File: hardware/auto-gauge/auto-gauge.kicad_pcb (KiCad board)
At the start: 2 copper layers, 48.6 x 48.3 mm, 41 parts

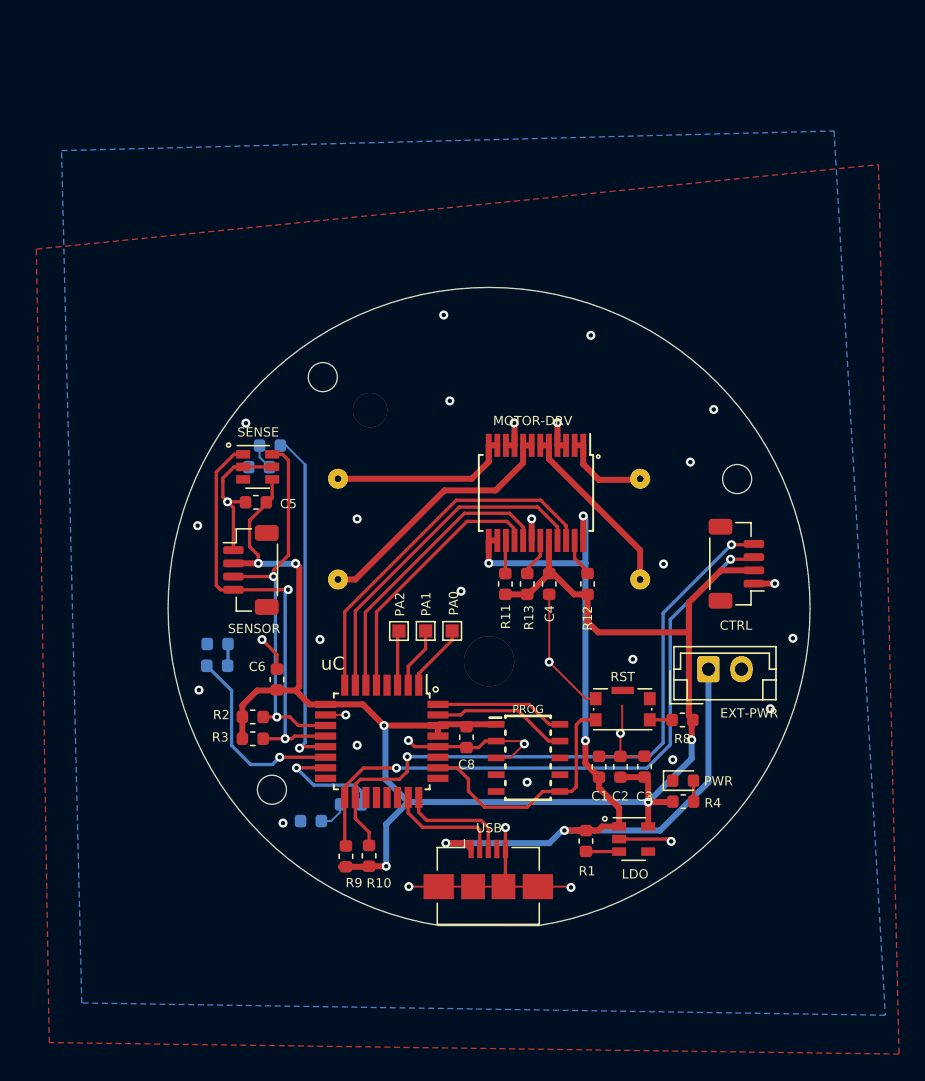
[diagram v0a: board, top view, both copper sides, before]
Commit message: arduino dummy/test. New board using atmega328 for jlcpcb asm
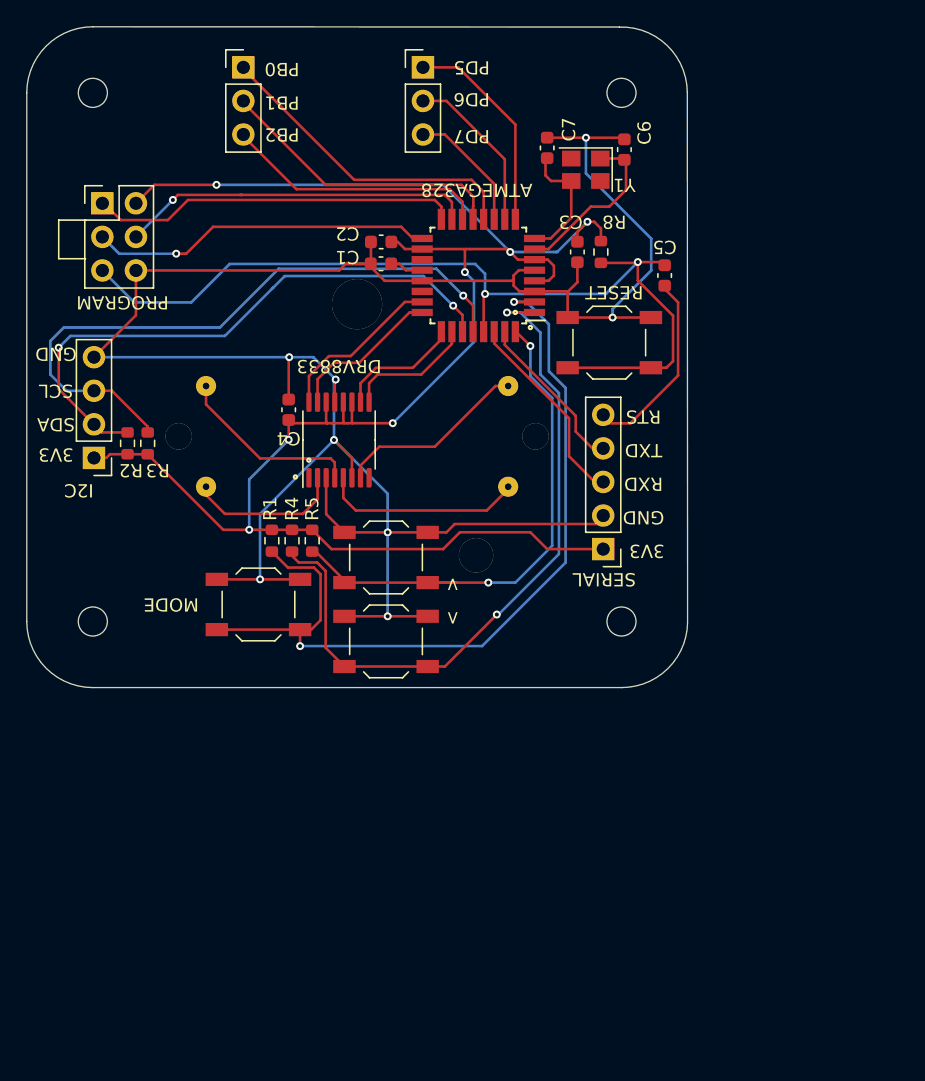
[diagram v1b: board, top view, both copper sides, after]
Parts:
- removed C8: 1uF, Capacitor_SMD:C_0603_1608Metric
- removed CTRL: CONN_04JST-SH, Connector_JST:JST_SH_BM04B-SRSS-TB_1x04-1MP_P1.00mm_Vertical
- removed D1, D2, D3, PWR: LED, LED_SMD:LED_0603_1608Metric
- removed EXT-PWR: JST Vertical Header, Connector_JST:JST_EH_B2B-EH-A_1x02_P2.50mm_Vertical
- removed Gauge: Stepper_Motor_bipolar, auto-gauge:Auto-Stepper-Test
- removed LDO: SPX3819M5-L-3-3, Package_TO_SOT_SMD:SOT-23-5
- removed MOTOR-DRV: TB6612FNG, Package_SO:SSOP-24_5.3x8.2mm_P0.65mm
- removed PA0, PA1, PA2: TestPoint, TestPoint:TestPoint_Pad_1.0x1.0mm
- removed PROG: CORTEX_DEBUG_SMD, sf:SAMTECH_FTSH-105-01
- removed R10, R9: 4.7k, Resistor_SMD:R_0603_1608Metric
- removed R11, R12, R13: 10k, Resistor_SMD:R_0603_1608Metric
- removed R6, R7: 1.5k, Resistor_SMD:R_0603_1608Metric
- removed RST: SW_Push, Button_Switch_SMD:SW_Push_1P1T-SH_NO_CK_KMR2xxG
- removed SENSE: TMP101, Package_TO_SOT_SMD:SOT-23-6
- removed SENSOR: CONN_04JST-PTH, Connector_JST:JST_SH_BM04B-SRSS-TB_1x04-1MP_P1.00mm_Vertical
- removed USB: USB_B_Micro, Connector_USB:USB_Micro-B_Amphenol_10104110_Horizontal
- removed uC: ATSAMD21E16B-A, Package_QFP:TQFP-32_7x7mm_P0.8mm
- added C7: 6pF, Capacitor_SMD:C_0603_1608Metric, F.Cu at (214.4, 74.2)
- added DOWN1: SW_Push, Button_Switch_SMD:SW_SPST_TL3342, F.Cu at (202.2, 105.2)
- added Gauge1: Stepper_Motor_bipolar, auto-gauge:Auto-Stepper-Test, F.Cu at (200.0, 90.0)
- added H4: MountingHole, MountingHole:MountingHole_2.2mm_M2, F.Cu at (220.0, 110.0)
- added I2C1: Conn_01x04, Connector_PinHeader_2.54mm:PinHeader_1x04_P2.54mm_Vertical, F.Cu at (180.1, 97.6)
- added J1: Conn_01x03, Connector_PinHeader_2.54mm:PinHeader_1x03_P2.54mm_Vertical, F.Cu at (191.4, 68.1)
- added J2: Conn_01x03, Connector_PinHeader_2.54mm:PinHeader_1x03_P2.54mm_Vertical, F.Cu at (205.0, 68.1)
- added MODE1: SW_Push, Button_Switch_SMD:SW_SPST_TL3342, F.Cu at (192.5, 108.7)
- added PROG1: Conn_02x03_Odd_Even, Connector_PinHeader_2.54mm:PinHeader_2x03_P2.54mm_Vertical, F.Cu at (180.7, 78.4)
- added RST1: SW_Push, Button_Switch_SMD:SW_SPST_TL3342, F.Cu at (219.1, 88.9)
- added SERIAL1: Conn_01x05, Connector_PinHeader_2.54mm:PinHeader_1x05_P2.54mm_Vertical, F.Cu at (218.6, 104.5)
- added U1: DRV8833PW, Package_SO:TSSOP-16_4.4x5mm_P0.65mm, F.Cu at (198.6, 96.3)
- added U2: ATmega328P-AU, Package_QFP:TQFP-32_7x7mm_P0.8mm, F.Cu at (209.2, 83.8)
- added UP1: SW_Push, Button_Switch_SMD:SW_SPST_TL3342, F.Cu at (202.2, 111.5)
- added Y1: Crystal_GND24, Crystal:Crystal_SMD_Abracon_ABM8G-4Pin_3.2x2.5mm, F.Cu at (217.3, 75.8)
- C1, C2, C4: value 10uF -> 0.1uF
- C3, C5: value 1uF -> 0.1uF
- C6: value 1uF -> 6pF
- R1: value 4.7k -> 10k
- R4: value 2.1k -> 10k
- R5: value 1.5k -> 10k; moved to F.Cu
- moved C6 47.9 mm to (220.2, 74.3)
- moved C2 43.6 mm to (201.8, 81.3), turned to 180 degrees
- moved C1 41.5 mm to (201.8, 82.9), turned to 180 degrees
- moved C3 39.3 mm to (216.7, 82.0), turned to 270 degrees
- moved R8 35.9 mm to (218.4, 82.0), turned to 270 degrees
- moved R4 35.6 mm to (195.1, 103.9), turned to 270 degrees
- moved C5 35.4 mm to (223.3, 83.8), turned to 270 degrees
- moved R1 32.9 mm to (193.5, 103.9)
- moved H1 30.5 mm to (220.0, 70.0)
- moved H2 27.7 mm to (180.0, 70.0)
- moved R3 23.7 mm to (184.2, 96.5), turned to 90 degrees
- moved C4 23.7 mm to (194.8, 94.0), turned to 90 degrees
- moved R2 22.8 mm to (182.6, 96.5), turned to 90 degrees
- moved R5 20.2 mm to (196.6, 103.9), turned to 270 degrees
- moved H3 18.6 mm to (180.0, 110.0)
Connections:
- C1 pad 1: +5V -> /AREF
- C5 pad 1: +3V3 -> /nRESET
- C5 pad 2: GND -> /RTS
- C6 pad 1: +3V3 -> /XTAL1
- R1 pad 1: +5V -> +3V3
- R1 pad 2: Net-(LDO1-Pad3) -> /PD4
- R4 pad 2: Net-(PWR_LED1-Pad2) -> /PD3
- R5 pad 1: /LED1 -> +3V3
- R5 pad 2: Net-(D1-Pad2) -> /PD2
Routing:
- net GND: track 74.0 -> 177.2 mm, vias 34 -> 8
- net +5V: track 73.5 -> 0.00 mm, vias 5 -> 0
- net /PD4: track 0.00 -> 63.4 mm, vias 0 -> 2
- net /PD3: track 0.00 -> 53.5 mm, vias 0 -> 2
- net /nRESET: track 20.9 -> 70.2 mm, vias 0 -> 2
- net /SCL_SLAVE: track 49.1 -> 0.00 mm, vias 2 -> 0
- net /SDA_SLAVE: track 48.2 -> 0.00 mm, vias 2 -> 0
- net /PD2: track 0.00 -> 40.0 mm, vias 0 -> 2
- net /MISO: track 0.00 -> 28.0 mm
- net /MOSI: track 0.00 -> 26.9 mm, vias 0 -> 1
- net /LED3: track 26.1 -> 0.00 mm, vias 1 -> 0
- net /SCK: track 0.00 -> 25.9 mm, vias 0 -> 1
- net /PB0: track 0.00 -> 24.3 mm
- net /PB1: track 0.00 -> 22.3 mm
- net /PB2: track 0.00 -> 20.1 mm
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- removed copper zone on B.Cu, net GND
- removed copper zone on F.Cu, net GND
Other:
- board size 48.6 x 48.3 mm -> 50 x 50 mm
- copper layers 2 -> 4
- net class Default: clearance 0.1524 -> 0.127; trace_width 0.1524 -> 0.127; via_dia 0.6858 -> 0.6; via_drill 0.3302 -> 0.3
- rule pad_to_mask_clearance: 0.0508 -> 0
- rule solder_mask_min_width: 0.101 -> 0.12
- rule trace_clearance: 0.1524 -> 0.127
- rule trace_min: 0.1524 -> 0.127
- rule via_min_drill: 0.254 -> 0.3
- rule via_min_size: 0.508 -> 0.6
- board text added: "3V3"
- board text added: "<"
- board text added: ">"
- board text added: "ATMEGA328"
- board text added: "DRV8833"
- board text added: "GND"
- board text added: "I2C"
- board text added: "MODE"
- board text added: "PB0"
- board text added: "PB1"
- board text added: "PB2"
- board text added: "PD5"
- board text added: "PD6"
- board text added: "PD7"
- board text added: "PROGRAM"
- board text added: "RESET"
- board text added: "RTS"
- board text added: "RXD"
- board text added: "SCL"
- board text added: "SDA"
- board text added: "SERIAL"
- board text added: "TXD"

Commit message: gnd pour, remove middle layers, DRC for jlcpcb
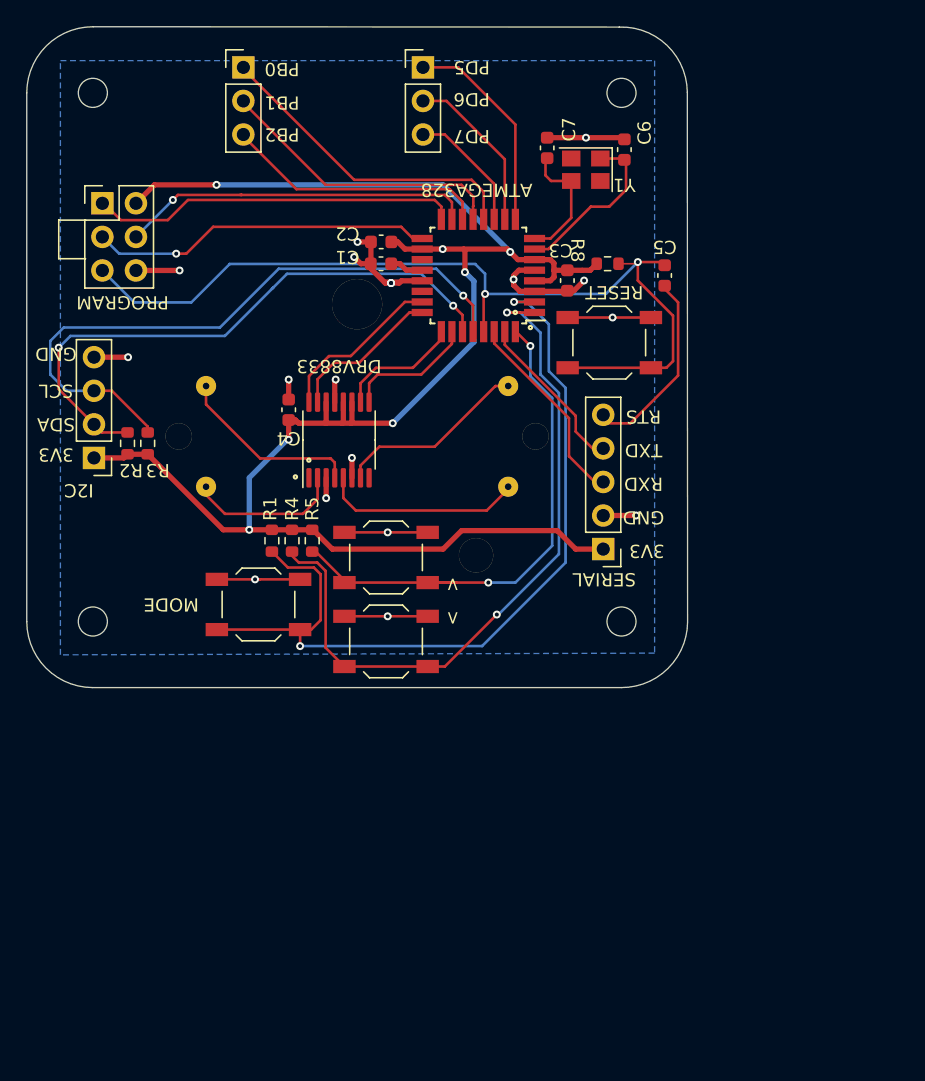
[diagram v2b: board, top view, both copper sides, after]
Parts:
- moved C3 2.29 mm to (215.9, 84.2)
- moved R8 1.02 mm to (218.9, 82.9), turned to 0 degrees
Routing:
- net GND: track 177.2 -> 75.5 mm, vias 8 -> 18
- net +3V3: track 141.9 -> 159.4 mm
- net /nRESET: track 70.2 -> 69.0 mm
- net /AREF: track 2.54 -> 3.20 mm
- added copper zone on B.Cu, net GND
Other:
- copper layers 4 -> 2
- rule via_min_drill: 0.3 -> 0.2
- rule via_min_size: 0.6 -> 0.4

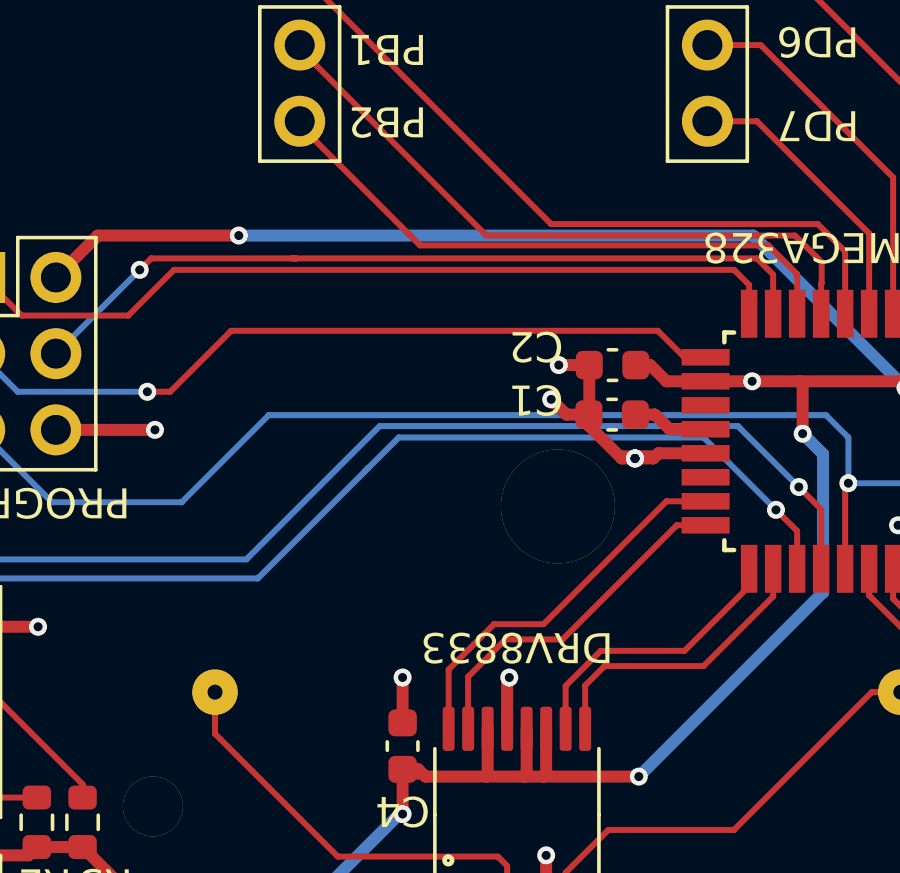
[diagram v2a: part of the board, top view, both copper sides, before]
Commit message: add brewbutler logo to silkscreens
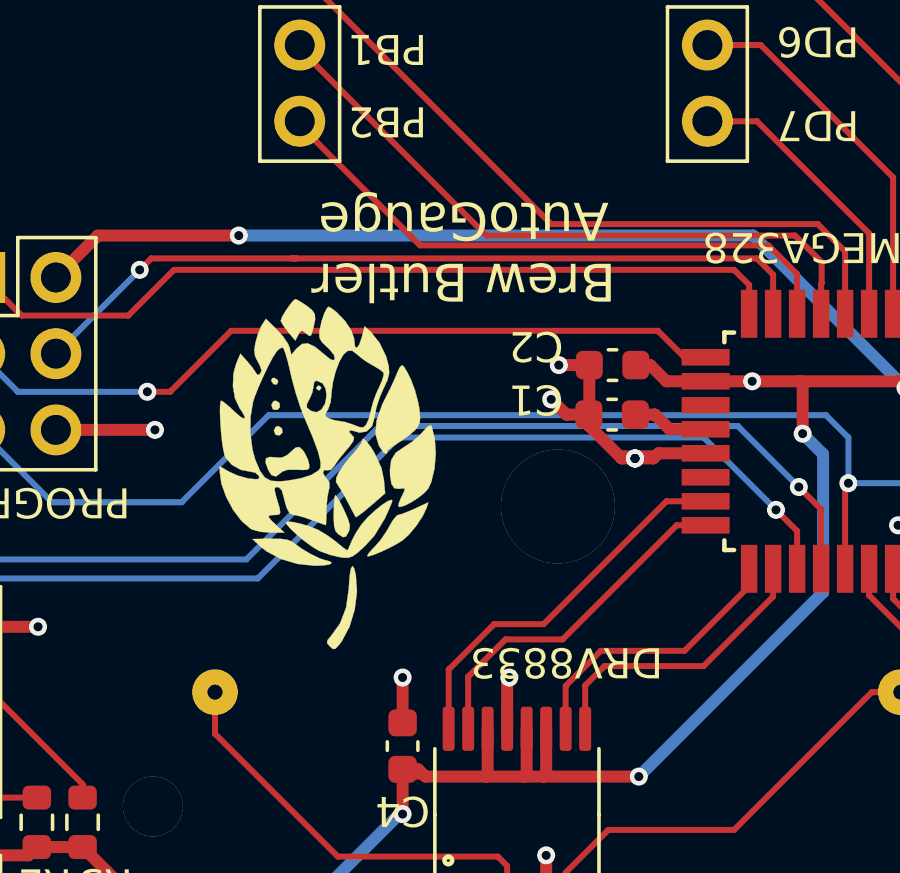
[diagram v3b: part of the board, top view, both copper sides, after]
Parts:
- added G***: LOGO, auto-gauge:butler, F.Cu at (192.0, 83.8)
- added G***: LOGO, auto-gauge:butler, B.Cu at (211.7, 75.6)
- added G***: LOGO, auto-gauge:butler, F.Cu at (181.6, 104.3)
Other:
- board text added: "Brew Butler AutoGauge"

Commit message: Ordered from JLCPCB
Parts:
- removed the G*** at (211.7, 75.6)
- turned G*** to 0 degrees
